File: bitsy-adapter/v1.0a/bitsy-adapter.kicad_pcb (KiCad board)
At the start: 2 copper layers, 75 x 35 mm, 28 parts, among them J1 PMOD1, J2 PMOD2, J3 PMOD3, J4 5V AUX, J5 5V AUX

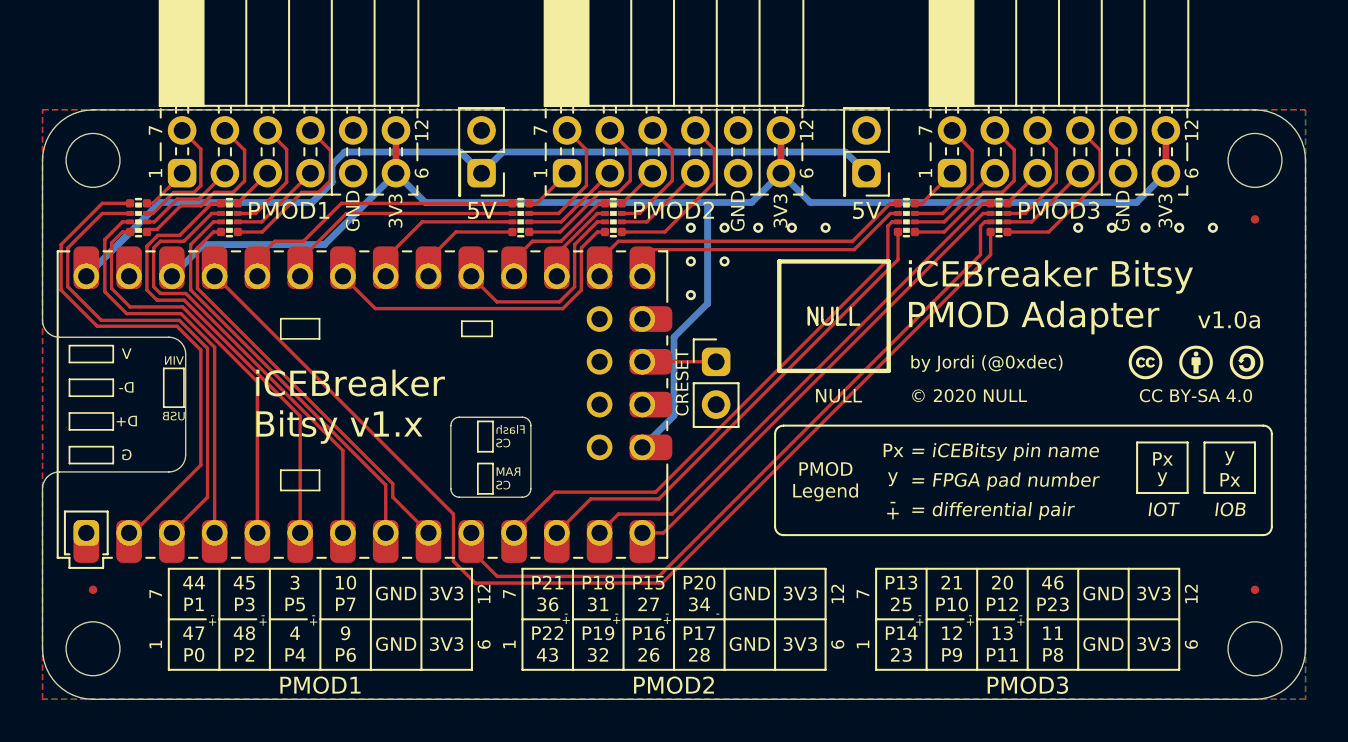
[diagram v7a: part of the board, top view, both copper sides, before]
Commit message: Bitsy Adapter: increase board size to accomadate better grounding
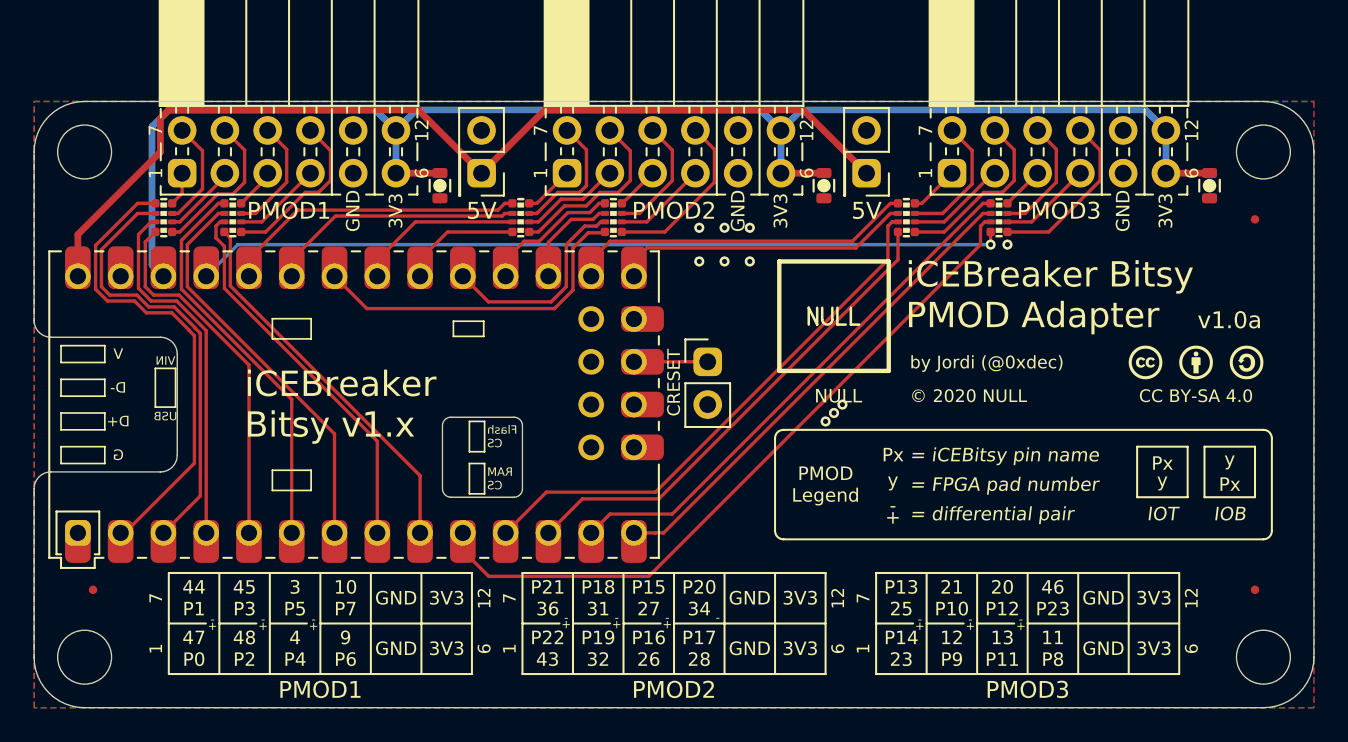
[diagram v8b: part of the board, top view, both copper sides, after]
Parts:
- added C1: 1u, pkl_dipol:C_0603, F.Cu at (86.1, 87.0)
- added C2: 1u, pkl_dipol:C_0603, F.Cu at (108.9, 87.0)
- added C3: 1u, pkl_dipol:C_0603, F.Cu at (131.8, 87.0)
- moved R1 1.50 mm to (69.7, 88.9)
- moved H1 0.71 mm to (65.0, 115.0)
- moved H2 0.71 mm to (65.0, 85.0)
- moved H3 0.71 mm to (135.0, 115.0)
- moved H4 0.71 mm to (135.0, 85.0)
- moved A1 0.50 mm to (81.0, 100.0)
- moved JP1 0.50 mm to (102.0, 97.5)
- moved R2 0.20 mm to (73.8, 88.9)
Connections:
- A1 pad 29: +3V3 -> Net-(A1-Pad29)
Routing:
- net /P23: track 64.7 -> 48.1 mm, vias 0 -> 1
- net +5V: track 51.6 -> 58.2 mm
- net /P4: track 27.2 -> 23.5 mm
- net /P5: track 27.3 -> 23.7 mm
- net /P0: track 30.4 -> 27.9 mm
- net /P3: track 24.0 -> 21.6 mm
- net /P1: track 28.5 -> 26.1 mm
- net /P2: track 23.9 -> 21.6 mm
- net /P7: track 24.4 -> 22.7 mm
- net /P6: track 24.3 -> 22.8 mm
- net /J1P8: track 10.5 -> 9.09 mm
- net /J1P2: track 5.83 -> 4.45 mm
- net /P13: track 16.8 -> 18.1 mm
- net /J1P7: track 7.62 -> 6.38 mm
- net /P15: track 4.67 -> 5.58 mm
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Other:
- board size 75 x 35 mm -> 76 x 36 mm
